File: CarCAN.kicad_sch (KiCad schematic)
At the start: 19 parts, among them J11 CAN_In, J12 CAN_Out, U4 ADM3055E, U5 CDSOT23-T24CAN

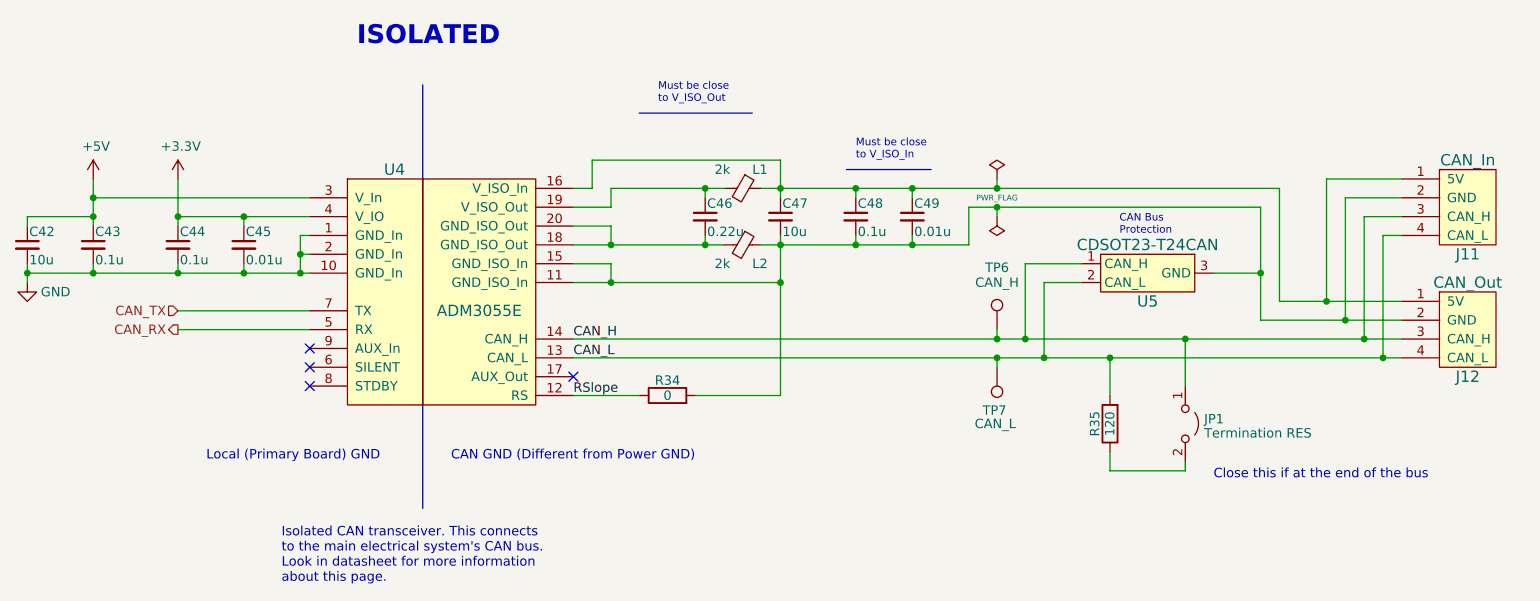
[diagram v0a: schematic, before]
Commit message: inputs routing + fixed models + clock keepouts
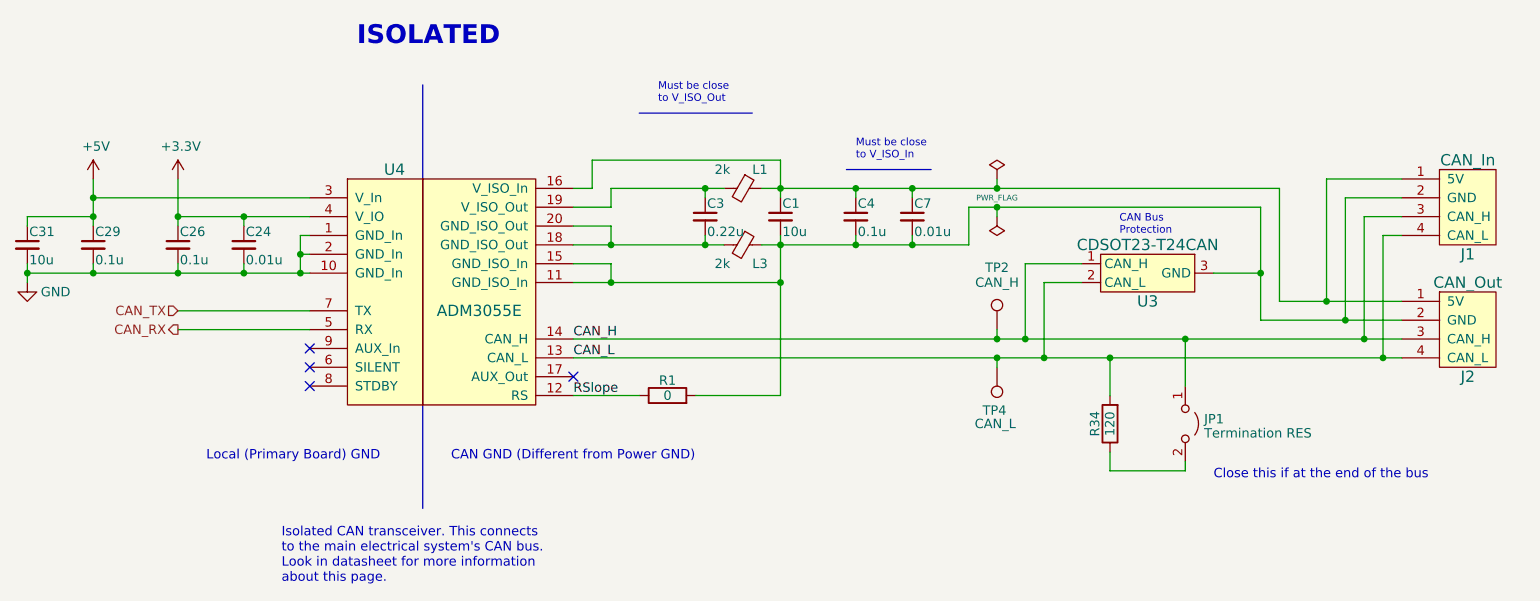
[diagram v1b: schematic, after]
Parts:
- renumbered C47 to C1, C45 to C24, C44 to C26, C43 to C29, C46 to C3, C42 to C31, C48 to C4, C49 to C7, J11 to J1, J12 to J2, L2 to L3, R34 to R1, R35 to R34, TP6 to TP2, TP7 to TP4, U5 to U3
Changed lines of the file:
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@@
   (symbol (lib_id "utsvt-connectors:CANConnector") (at 248.92 96.52 0) (mirror y) (unit 1)
     (in_bom yes) (on_board yes) (dnp no)
-    (property "Reference" "J12" (at 248.92 102.87 0)
+    (property "Reference" "J2" (at 248.92 102.87 0)
       (effects (font (size 1.524 1.524)))
     )
@@
       (project "Telemetry-Primary"
         (path "/7f2a449b-14af-42b3-8d38-5f0f8a5ee7ce/00000000-0000-0000-0000-00005f693e58"
-          (reference "J12") (unit 1)
+          (reference "J2") (unit 1)
         )
         (path "/7f2a449b-14af-42b3-8d38-5f0f8a5ee7ce/3478efb6-187c-4b5f-bbc8-4ecfc76c057f"
@@
   (symbol (lib_id "Device:R") (at 200.66 109.22 180) (unit 1)
     (in_bom yes) (on_board yes) (dnp no)
-    (property "Reference" "R35" (at 198.628 109.22 90)
+    (property "Reference" "R34" (at 198.628 109.22 90)
       (effects (font (size 1.27 1.27)))
     )
@@
       (project "Telemetry-Primary"
         (path "/7f2a449b-14af-42b3-8d38-5f0f8a5ee7ce/00000000-0000-0000-0000-00005f693e58"
-          (reference "R35") (unit 1)
+          (reference "R34") (unit 1)
         )
         (path "/7f2a449b-14af-42b3-8d38-5f0f8a5ee7ce/3478efb6-187c-4b5f-bbc8-4ecfc76c057f"
@@
   (symbol (lib_id "Device:C_Small") (at 54.61 85.09 0) (unit 1)
     (in_bom yes) (on_board yes) (dnp no)
-    (property "Reference" "C42" (at 54.864 83.312 0)
+    (property "Reference" "C31" (at 54.864 83.312 0)
       (effects (font (size 1.27 1.27)) (justify left))
     )
@@
       (project "Telemetry-Primary"
         (path "/7f2a449b-14af-42b3-8d38-5f0f8a5ee7ce/00000000-0000-0000-0000-00005f693e58"
-          (reference "C42") (unit 1)
+          (reference "C31") (unit 1)
         )
         (path "/7f2a449b-14af-42b3-8d38-5f0f8a5ee7ce/3478efb6-187c-4b5f-bbc8-4ecfc76c057f"
@@
   (symbol (lib_id "Device:C_Small") (at 63.5 85.09 0) (unit 1)
     (in_bom yes) (on_board yes) (dnp no)
-    (property "Reference" "C43" (at 63.754 83.312 0)
+    (property "Reference" "C29" (at 63.754 83.312 0)
       (effects (font (size 1.27 1.27)) (justify left))
     )
@@
       (project "Telemetry-Primary"
         (path "/7f2a449b-14af-42b3-8d38-5f0f8a5ee7ce/00000000-0000-0000-0000-00005f693e58"
-          (reference "C43") (unit 1)
+          (reference "C29") (unit 1)
         )
         (path "/7f2a449b-14af-42b3-8d38-5f0f8a5ee7ce/3478efb6-187c-4b5f-bbc8-4ecfc76c057f"
@@
   (symbol (lib_id "Device:C_Small") (at 74.93 85.09 0) (unit 1)
     (in_bom yes) (on_board yes) (dnp no)
-    (property "Reference" "C44" (at 75.184 83.312 0)
+    (property "Reference" "C26" (at 75.184 83.312 0)
       (effects (font (size 1.27 1.27)) (justify left))
     )
@@
       (project "Telemetry-Primary"
         (path "/7f2a449b-14af-42b3-8d38-5f0f8a5ee7ce/00000000-0000-0000-0000-00005f693e58"
-          (reference "C44") (unit 1)
+          (reference "C26") (unit 1)
         )
         (path "/7f2a449b-14af-42b3-8d38-5f0f8a5ee7ce/3478efb6-187c-4b5f-bbc8-4ecfc76c057f"
@@
   (symbol (lib_id "Device:C_Small") (at 83.82 85.09 0) (unit 1)
     (in_bom yes) (on_board yes) (dnp no)
-    (property "Reference" "C45" (at 84.074 83.312 0)
+    (property "Reference" "C24" (at 84.074 83.312 0)
       (effects (font (size 1.27 1.27)) (justify left))
     )
@@
       (project "Telemetry-Primary"
         (path "/7f2a449b-14af-42b3-8d38-5f0f8a5ee7ce/00000000-0000-0000-0000-00005f693e58"
-          (reference "C45") (unit 1)
+          (reference "C24") (unit 1)
         )
         (path "/7f2a449b-14af-42b3-8d38-5f0f8a5ee7ce/3478efb6-187c-4b5f-bbc8-4ecfc76c057f"
@@
   (symbol (lib_id "Device:C_Small") (at 156.21 81.28 0) (unit 1)
     (in_bom yes) (on_board yes) (dnp no)
-    (property "Reference" "C47" (at 156.464 79.502 0)
+    (property "Reference" "C1" (at 156.464 79.502 0)
       (effects (font (size 1.27 1.27)) (justify left))
     )
@@
       (project "Telemetry-Primary"
         (path "/7f2a449b-14af-42b3-8d38-5f0f8a5ee7ce/00000000-0000-0000-0000-00005f693e58"
-          (reference "C47") (unit 1)
+          (reference "C1") (unit 1)
         )
         (path "/7f2a449b-14af-42b3-8d38-5f0f8a5ee7ce/3478efb6-187c-4b5f-bbc8-4ecfc76c057f"
@@
   (symbol (lib_id "Device:C_Small") (at 146.05 81.28 0) (unit 1)
     (in_bom yes) (on_board yes) (dnp no)
-    (property "Reference" "C46" (at 146.304 79.502 0)
+    (property "Reference" "C3" (at 146.304 79.502 0)
       (effects (font (size 1.27 1.27)) (justify left))
     )
@@
       (project "Telemetry-Primary"
         (path "/7f2a449b-14af-42b3-8d38-5f0f8a5ee7ce/00000000-0000-0000-0000-00005f693e58"
-          (reference "C46") (unit 1)
+          (reference "C3") (unit 1)
         )
         (path "/7f2a449b-14af-42b3-8d38-5f0f8a5ee7ce/3478efb6-187c-4b5f-bbc8-4ecfc76c057f"
@@
   (symbol (lib_id "Device:FerriteBead_Small") (at 151.13 85.09 270) (unit 1)
     (in_bom yes) (on_board yes) (dnp no)
-    (property "Reference" "L2" (at 152.4 87.63 90)
+    (property "Reference" "L3" (at 152.4 87.63 90)
       (effects (font (size 1.27 1.27)) (justify left))
     )
@@
       (project "Telemetry-Primary"
         (path "/7f2a449b-14af-42b3-8d38-5f0f8a5ee7ce/00000000-0000-0000-0000-00005f693e58"
-          (reference "L2") (unit 1)
+          (reference "L3") (unit 1)
         )
         (path "/7f2a449b-14af-42b3-8d38-5f0f8a5ee7ce/3478efb6-187c-4b5f-bbc8-4ecfc76c057f"
@@
   (symbol (lib_id "Device:C_Small") (at 166.37 81.28 0) (unit 1)
     (in_bom yes) (on_board yes) (dnp no)
-    (property "Reference" "C48" (at 166.624 79.502 0)
+    (property "Reference" "C4" (at 166.624 79.502 0)
       (effects (font (size 1.27 1.27)) (justify left))
     )
@@
       (project "Telemetry-Primary"
         (path "/7f2a449b-14af-42b3-8d38-5f0f8a5ee7ce/00000000-0000-0000-0000-00005f693e58"
-          (reference "C48") (unit 1)
+          (reference "C4") (unit 1)
         )
         (path "/7f2a449b-14af-42b3-8d38-5f0f8a5ee7ce/3478efb6-187c-4b5f-bbc8-4ecfc76c057f"
@@
   (symbol (lib_id "Device:C_Small") (at 173.99 81.28 0) (unit 1)
     (in_bom yes) (on_board yes) (dnp no)
-    (property "Reference" "C49" (at 174.244 79.502 0)
+    (property "Reference" "C7" (at 174.244 79.502 0)
       (effects (font (size 1.27 1.27)) (justify left))
     )
@@
       (project "Telemetry-Primary"
         (path "/7f2a449b-14af-42b3-8d38-5f0f8a5ee7ce/00000000-0000-0000-0000-00005f693e58"
-          (reference "C49") (unit 1)
+          (reference "C7") (unit 1)
         )
         (path "/7f2a449b-14af-42b3-8d38-5f0f8a5ee7ce/3478efb6-187c-4b5f-bbc8-4ecfc76c057f"
@@
   (symbol (lib_id "utsvt-chips:CDSOT23-T24CAN") (at 205.74 88.9 0) (unit 1)
     (in_bom yes) (on_board yes) (dnp no)
-    (property "Reference" "U5" (at 205.74 92.71 0)
+    (property "Reference" "U3" (at 205.74 92.71 0)
       (effects (font (size 1.524 1.524)))
     )
@@
       (project "Telemetry-Primary"
         (path "/7f2a449b-14af-42b3-8d38-5f0f8a5ee7ce/00000000-0000-0000-0000-00005f693e58"
-          (reference "U5") (unit 1)
+          (reference "U3") (unit 1)
         )
         (path "/7f2a449b-14af-42b3-8d38-5f0f8a5ee7ce/3478efb6-187c-4b5f-bbc8-4ecfc76c057f"
@@
   (symbol (lib_id "Connector:TestPoint") (at 185.42 96.52 0) (unit 1)
     (in_bom yes) (on_board yes) (dnp no)
-    (property "Reference" "TP6" (at 185.42 88.9 0)
+    (property "Reference" "TP2" (at 185.42 88.9 0)
       (effects (font (size 1.27 1.27)) (justify bottom))
     )
@@
       (project "Telemetry-Primary"
         (path "/7f2a449b-14af-42b3-8d38-5f0f8a5ee7ce/00000000-0000-0000-0000-00005f693e58"
-          (reference "TP6") (unit 1)
+          (reference "TP2") (unit 1)
         )
         (path "/7f2a449b-14af-42b3-8d38-5f0f8a5ee7ce/3478efb6-187c-4b5f-bbc8-4ecfc76c057f"
@@
   (symbol (lib_id "Connector:TestPoint") (at 185.42 101.6 180) (unit 1)
     (in_bom yes) (on_board yes) (dnp no)
-    (property "Reference" "TP7" (at 186.69 106.68 0)
+    (property "Reference" "TP4" (at 186.69 106.68 0)
       (effects (font (size 1.27 1.27)) (justify left bottom))
     )
@@
       (project "Telemetry-Primary"
         (path "/7f2a449b-14af-42b3-8d38-5f0f8a5ee7ce/00000000-0000-0000-0000-00005f693e58"
-          (reference "TP7") (unit 1)
+          (reference "TP4") (unit 1)
         )
         (path "/7f2a449b-14af-42b3-8d38-5f0f8a5ee7ce/3478efb6-187c-4b5f-bbc8-4ecfc76c057f"
@@
   (symbol (lib_id "Device:R") (at 140.97 105.41 90) (unit 1)
     (in_bom yes) (on_board yes) (dnp no)
-    (property "Reference" "R34" (at 140.97 103.378 90)
+    (property "Reference" "R1" (at 140.97 103.378 90)
       (effects (font (size 1.27 1.27)))
     )
@@
       (project "Telemetry-Primary"
         (path "/7f2a449b-14af-42b3-8d38-5f0f8a5ee7ce/00000000-0000-0000-0000-00005f693e58"
-          (reference "R34") (unit 1)
+          (reference "R1") (unit 1)
         )
         (path "/7f2a449b-14af-42b3-8d38-5f0f8a5ee7ce/3478efb6-187c-4b5f-bbc8-4ecfc76c057f"
@@
   (symbol (lib_id "utsvt-connectors:CANConnector") (at 248.92 80.01 0) (mirror y) (unit 1)
     (in_bom yes) (on_board yes) (dnp no)
-    (property "Reference" "J11" (at 248.92 86.36 0)
+    (property "Reference" "J1" (at 248.92 86.36 0)
       (effects (font (size 1.524 1.524)))
     )
@@
       (project "Telemetry-Primary"
         (path "/7f2a449b-14af-42b3-8d38-5f0f8a5ee7ce/00000000-0000-0000-0000-00005f693e58"
-          (reference "J11") (unit 1)
-        )
-        (path "/7f2a449b-14af-42b3-8d38-5f0f8a5ee7ce/3478efb6-187c-4b5f-bbc8-4ecfc76c057f"
+          (reference "J1") (unit 1)
+        )
+        (path "/7f2a449b-14af-42b3-8d38-5f0f8a5ee7ce/3478efb6-187c-4b5f-bbc8-4ecfc76c057f"
